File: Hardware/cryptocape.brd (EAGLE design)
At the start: 86.4 x 54.6 mm, 50 parts, among them J1 AVR_SPI_PRG_6PTH, U2 ATMEGA328P, U3 EEPROM-I2CSMD, Y1 16MHz

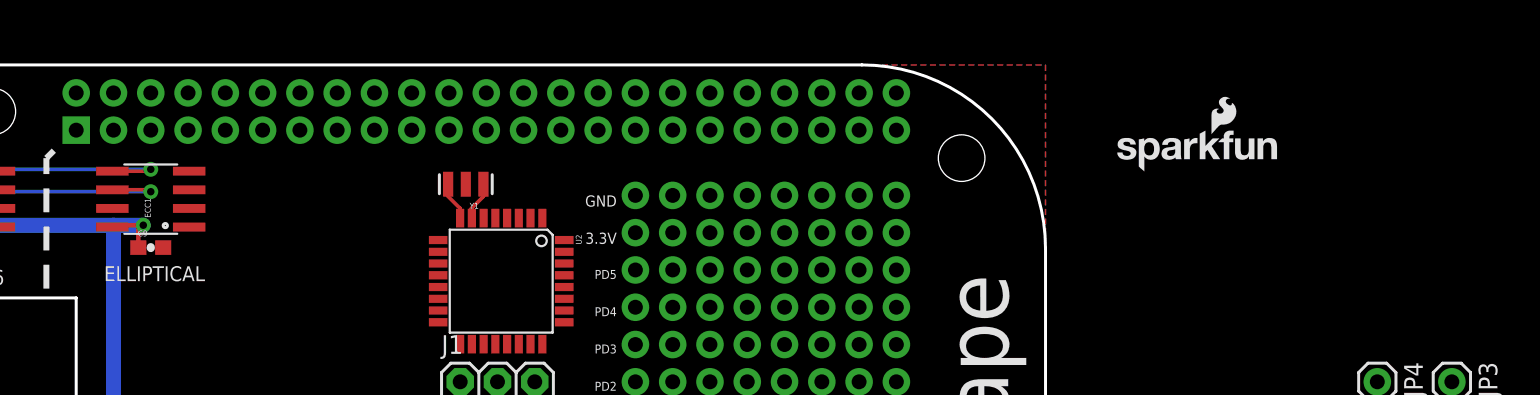
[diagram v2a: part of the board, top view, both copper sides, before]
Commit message: Adds ATAES123 and Cryptotronix Logo
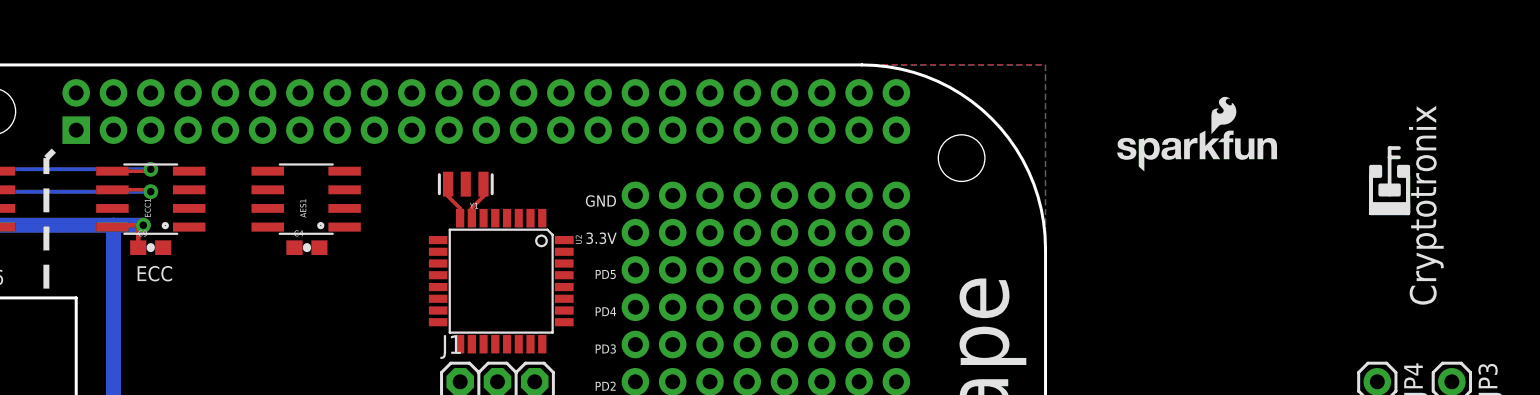
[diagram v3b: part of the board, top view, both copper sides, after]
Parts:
- added AES1: ATAES132, cryptotronix:SOIC8
- added C4: 0.1uF, SparkFun-Capacitors:0603-CAP
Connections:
- new net AUTH0: AES1.2, U$2.P8.11
- net 3.3V: now also AES1.8, C4.1
- net GND: now also AES1.4, C4.2
- net I2C2_SCL: now also AES1.6
- net I2C2_SDA: now also AES1.5
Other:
- board text added: "Cryptotronix"
- board text added: "ECC"
- board text removed: "ELLIPTICAL"
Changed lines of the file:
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@@
 <text x="12.7" y="40.64" size="1.016" layer="21" font="vector" ratio="15" rot="R180" align="bottom-center">SHA-256</text>
 <wire x1="18.288" y1="39.37" x2="18.288" y2="48.26" width="0.4064" layer="21" style="shortdash"/>
-<text x="25.654" y="39.878" size="1.016" layer="21" font="vector" ratio="15" align="bottom-center">ELLIPTICAL</text>
+<text x="25.654" y="39.878" size="1.016" layer="21" font="vector" ratio="15" align="bottom-center">ECC</text>
 <text x="15.748" y="6.604" size="1.524" layer="21" font="vector" ratio="15" align="bottom-center">RTC</text>
 <text x="28.702" y="8.382" size="1.27" layer="21" font="vector" ratio="16">WP</text>
@@
 <wire x1="48.26" y1="20.574" x2="32.004" y2="20.574" width="0.4064" layer="21" style="shortdash"/>
 <wire x1="18.288" y1="48.26" x2="18.796" y2="48.768" width="0.4064" layer="21" style="shortdash"/>
+<polygon width="0.254" layer="21">
+<vertex x="108.5342" y="44.5008"/>
+<vertex x="111.0742" y="44.5008"/>
+<vertex x="111.0742" y="45.1358"/>
+<vertex x="108.5342" y="45.1358"/>
+</polygon>
+<polygon width="0.254" layer="21">
+<vertex x="108.5342" y="44.5008"/>
+<vertex x="108.5342" y="47.0408"/>
+<vertex x="109.1692" y="47.0408"/>
+<vertex x="109.1692" y="47.6758"/>
+<vertex x="108.5342" y="47.6758"/>
+</polygon>
+<polygon width="0.254" layer="21">
+<vertex x="111.0742" y="44.5008"/>
+<vertex x="111.0742" y="47.6758"/>
+<vertex x="110.4392" y="47.6758"/>
+<vertex x="110.4392" y="47.0408"/>
+<vertex x="111.0742" y="47.0408"/>
+</polygon>
+<polygon width="0.254" layer="21">
+<vertex x="109.1692" y="45.7708"/>
+<vertex x="110.4392" y="45.7708"/>
+<vertex x="110.4392" y="46.4058"/>
+<vertex x="109.1692" y="46.4058"/>
+</polygon>
+<wire x1="109.8042" y1="45.7708" x2="109.8042" y2="48.3108" width="0.254" layer="21"/>
+<wire x1="109.8042" y1="48.3108" x2="109.8042" y2="48.9458" width="0.254" layer="21"/>
+<wire x1="110.4392" y1="48.3108" x2="109.8042" y2="48.3108" width="0.254" layer="21"/>
+<wire x1="110.4392" y1="48.9458" x2="109.8042" y2="48.9458" width="0.254" layer="21"/>
+<text x="112.9792" y="38.1508" size="1.778" layer="21" font="vector" ratio="15" rot="R90">Cryptotronix</text>
 </plain>
 <attributes>
@@
 <element name="JP14" library="SparkFun-Passives" package="1X02" value="" x="16.764" y="19.05" rot="R180"/>
 <element name="U$6" library="SparkFun-Aesthetics" package="OSHW-LOGO-S" value="" x="9.525" y="51.435" rot="MR270"/>
+<element name="AES1" library="cryptotronix" package="SOIC8" value="ATAES132" x="35.9918" y="45.466" rot="R90"/>
+<element name="C4" library="SparkFun-Capacitors" package="0603-CAP" value="0.1uF" x="36.0426" y="42.164">
+<attribute name="PROD_ID" value="CAP-00810" x="36.0426" y="42.164" size="1.778" layer="27" display="off"/>
+</element>
 </elements>
 <signals>
@@
 <via x="12.192" y="18.034" extent="1-16" drill="0.508"/>
 <via x="13.208" y="8.89" extent="1-16" drill="0.508"/>
+<contactref element="AES1" pad="4"/>
+<contactref element="AES1" pad="4"/>
+<contactref element="C4" pad="2"/>
 <wire x1="118.237" y1="9.613" x2="119.7102" y2="12.192" width="0" layer="19" extent="1-1"/>
 <wire x1="116.713" y1="12.661" x2="119.7102" y2="12.192" width="0" layer="19" extent="1-1"/>
@@
 <wire x1="27.8384" y1="16.637" x2="28.3464" y2="16.129" width="0.2032" layer="1"/>
 <wire x1="28.3464" y1="16.129" x2="29.21" y2="16.129" width="0.2032" layer="1"/>
+<contactref element="AES1" pad="6"/>
 <wire x1="58.42" y1="30.48" x2="53.5686" y2="39.478" width="0" layer="19" extent="1-1"/>
+<wire x1="33.3756" y1="46.101" x2="53.5686" y2="39.478" width="0" layer="19" extent="1-1"/>
+<wire x1="25.4" y1="45.974" x2="33.3756" y2="46.101" width="0" layer="19" extent="1-1"/>
 <wire x1="36.83" y1="17.9324" x2="58.42" y2="30.48" width="0" layer="19" extent="1-1"/>
 <wire x1="29.21" y1="16.129" x2="36.83" y2="17.9324" width="0" layer="19" extent="1-1"/>
 <wire x1="43.18" y1="1.905" x2="36.83" y2="17.9324" width="0" layer="19" extent="1-1"/>
-<wire x1="25.4" y1="45.974" x2="53.5686" y2="39.478" width="0" layer="19" extent="1-1"/>
 </signal>
 <signal name="I2C2_SDA">
@@
 <wire x1="28.067" y1="17.145" x2="28.575" y2="16.637" width="0.2032" layer="1"/>
 <wire x1="28.575" y1="16.637" x2="29.21" y2="16.637" width="0.2032" layer="1"/>
+<contactref element="AES1" pad="5"/>
 <wire x1="58.42" y1="27.94" x2="53.5686" y2="38.678" width="0" layer="19" extent="1-1"/>
+<wire x1="33.3756" y1="47.371" x2="53.5686" y2="38.678" width="0" layer="19" extent="1-1"/>
+<wire x1="25.4" y1="47.498" x2="33.3756" y2="47.371" width="0" layer="19" extent="1-1"/>
 <wire x1="36.83" y1="18.5928" x2="58.42" y2="27.94" width="0" layer="19" extent="1-1"/>
 <wire x1="29.21" y1="16.637" x2="36.83" y2="18.5928" width="0" layer="19" extent="1-1"/>
 <wire x1="43.18" y1="4.445" x2="36.83" y2="18.5928" width="0" layer="19" extent="1-1"/>
-<wire x1="25.4" y1="47.498" x2="53.5686" y2="38.678" width="0" layer="19" extent="1-1"/>
 </signal>
 <signal name="SYS_RESET">
@@
 </polygon>
 <via x="39.751" y="15.875" extent="1-16" drill="0.508"/>
+<contactref element="AES1" pad="8"/>
+<contactref element="C4" pad="1"/>
 <wire x1="116.713" y1="10.961" x2="119.7102" y2="10.922" width="0" layer="19" extent="1-1"/>
 <wire x1="118.237" y1="7.913" x2="119.7102" y2="10.922" width="0" layer="19" extent="1-1"/>
@@
 <wire x1="47.276" y1="35.5854" x2="48.076" y2="44.1706" width="0" layer="19" extent="1-1"/>
 <wire x1="46.482" y1="33.02" x2="47.276" y2="35.5854" width="0" layer="19" extent="1-1"/>
-<wire x1="44.4872" y1="18.5928" x2="46.482" y2="33.02" width="0" layer="19" extent="1-1"/>
-<wire x1="30.226" y1="18.415" x2="35.267" y2="16.002" width="0" layer="19" extent="1-16"/>
+<wire x1="35.1926" y1="42.164" x2="48.076" y2="44.1706" width="0" layer="19" extent="1-1"/>
+<wire x1="33.3756" y1="43.561" x2="35.1926" y2="42.164" width="0" layer="19" extent="1-1"/>
+<wire x1="24.892" y1="43.688" x2="33.3756" y2="43.561" width="0" layer="19" extent="1-1"/>
+<wire x1="35.267" y1="16.002" x2="30.226" y2="18.415" width="0" layer="19" extent="1-16"/>
 </signal>
 <signal name="N$18">
@@
 <wire x1="58.42" y1="20.32" x2="51.276" y2="35.5854" width="0" layer="19" extent="1-1"/>
 </signal>
+<signal name="AUTH0">
+<contactref element="AES1" pad="2"/>
+<contactref element="U$2" pad="P8.11"/>
+<wire x1="33.02" y1="50.165" x2="38.608" y2="44.831" width="0" layer="19" extent="1-1"/>
+</signal>
 </signals>

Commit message: finished layout with lables.  Board is in state for review
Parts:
- removed JP10, JP11, JP12, JP9: M161X16_NO_SILK, SparkFun-Connectors:1X16_NO_SILK
- removed U$1: DS1077, SparkFun-FreqCtrl:SO08
- removed Y1: 16MHz, SparkFun-FreqCtrl:RESONATOR-SMD
- added C5: .1uf, SparkFun-Capacitors:0603-CAP
- added D1: GREEN, SparkFun-LED:LED-0603
- added R1: 10k, SparkFun-Resistors:0603-RES
- added R2: 1k, SparkFun-Resistors:0603-RES
- added U1: 33mhz, cryptotronix:CRYSTAL-OSC-SMD-5X3.2
- added Y2: 8MHZ, SparkFun-FreqCtrl:RESONATOR-SMD
- C10: value 10nF -> 0.1uF
- JP5: value M161X16_NO_SILK -> M11PTH; device SparkFun-Connectors:1X16_NO_SILK -> SparkFun-Connectors:1X11
- JP6: value M161X16_NO_SILK -> (none); device SparkFun-Connectors:1X16_NO_SILK -> SparkFun-Connectors:1X04
- JP7, JP8: value M161X16_NO_SILK -> M02PTH; device SparkFun-Connectors:1X16_NO_SILK -> SparkFun-Connectors:1X02
- moved C10 86.6 mm to (33.0, 34.0), turned to 270 degrees
- moved JP3 76.6 mm to (37.8, 25.4)
- moved C14 75.6 mm to (46.5, 32.5), turned to 0 degrees
- moved JP4 75.3 mm to (34.0, 25.4)
- moved U$4 37.3 mm to (80.5, 11.4), turned to 90 degrees
- moved JP6 35.3 mm to (47.0, 40.0)
- moved U$5 32.5 mm to (80.5, 23.4), turned to 270 degrees
- moved JP8 27.4 mm to (47.0, 27.3), turned to 270 degrees
- moved JP5 16.5 mm to (50.8, 22.2)
- moved C4 14.7 mm to (26.2, 31.2)
- moved AES1 14.5 mm to (26.2, 34.8)
- moved J1 13.6 mm to (38.1, 41.1), turned to 90 degrees
- moved U2 12.0 mm to (39.4, 33.0), turned to 180 degrees
- moved JP7 10.2 mm to (53.3, 6.99)
- moved C2 3.02 mm to (46.6, 10.7), turned to 270 degrees
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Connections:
- removed net PC0: JP5.6, U2.23
- removed net PC1: JP5.7, U2.24
- removed net PC2: JP5.8, U2.25
- removed net PD2: JP5.11, U2.32
- removed net PD3: JP5.12, U2.1
- removed net PD4: JP5.13, U2.2
- removed net PD5: JP5.14, U2.9
- new net A0: JP6.4, U2.23
- new net A1: JP6.3, U2.24
- new net A2: JP6.2, U2.25
- new net A3: JP6.1, U2.26
- new net D10: JP5.11, U2.14
- new net D2: JP5.3, U2.32
- new net D3: JP5.4, U2.1
- new net D4: JP5.5, U2.2
- new net D5: JP5.6, U2.9
- new net D6: JP5.7, U2.10
- new net D7: JP5.8, U2.11
- new net D8: JP5.9, U2.12
- new net D9: JP5.10, U2.13
- new net N$12: D1.A, R2.1
- net 3.3V: now also C5.1, JP5.2, R1.2, U1.4; no longer JP5.15, U$1.3
- net AT328P_RST: now also R1.1
- net D0: now also JP8.1
- net D0': no longer JP5.5
- net D1: now also JP8.2
- net D1': no longer JP5.4
- net GND: now also C5.2, D1.C, JP5.1, U1.2, Y2.2; no longer JP5.16, U$1.4, Y1.2
- net I2C2_SCL: now also JP7.1; no longer JP5.10
- net I2C2_SDA: now also JP7.2; no longer JP5.9
- net N$4: now also Y2.1; no longer Y1.1
- net N$5: now also Y2.3; no longer Y1.3
- net SCK: now also R2.2
- net TPM_CLK: now also U1.3; no longer U$1.1
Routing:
- net I2C2_SCL: track 34.3 -> 119.0 mm, vias 2 -> 5
- net I2C2_SDA: track 36.7 -> 118.3 mm, vias 2 -> 5
- net 3.3V: track 115.9 -> 184.6 mm, vias 7 -> 10
- net AT328P_RST: track 0.00 -> 54.2 mm, vias 0 -> 2
- net D1: track 0.00 -> 36.6 mm, vias 0 -> 1
- net D0: track 0.00 -> 32.9 mm, vias 0 -> 1
- net A0: track 0.00 -> 23.5 mm, vias 0 -> 1
- net A2: track 0.00 -> 22.8 mm, vias 0 -> 1
- net A1: track 0.00 -> 21.3 mm, vias 0 -> 1
- net AUTH0: track 0.00 -> 19.1 mm, vias 0 -> 1
- net A3: track 0.00 -> 18.8 mm, vias 0 -> 1
- net D10: track 0.00 -> 17.4 mm
- net D9: track 0.00 -> 15.4 mm
- net SCK: track 0.00 -> 14.2 mm, vias 0 -> 1
- net D1': track 0.00 -> 14.1 mm, vias 0 -> 1
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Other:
- board text added: "3.3v"
- board text added: "A2"
- board text added: "A3"
- board text added: "AES-128"
- board text added: "D0"
- board text added: "D1"
- board text added: "D10"
- board text added: "D13"
- board text added: "D2"
- board text added: "D3"
- board text added: "D4"
- board text added: "D5"
- board text added: "D6"
- board text added: "D7"
- board text added: "D8"
- board text added: "D9"
- board text added: "JUMPERS"
- board text added: "MEGA328"
- board text added: "PROGRAM"
- board text added: "SCL"
- board text added: "SDA"
- board text removed: "3.3V"
- board text removed: "D0'"
- board text removed: "D1'"
- board text removed: "I2C_SCL"
- board text removed: "I2C_SDA"
- board text removed: "PC0"
- board text removed: "PC1"
- board text removed: "PC2"
- board text removed: "PD2"
- board text removed: "PD3"
- board text removed: "PD4"
- board text removed: "PD5"
